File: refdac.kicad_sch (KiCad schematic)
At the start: 2 parts

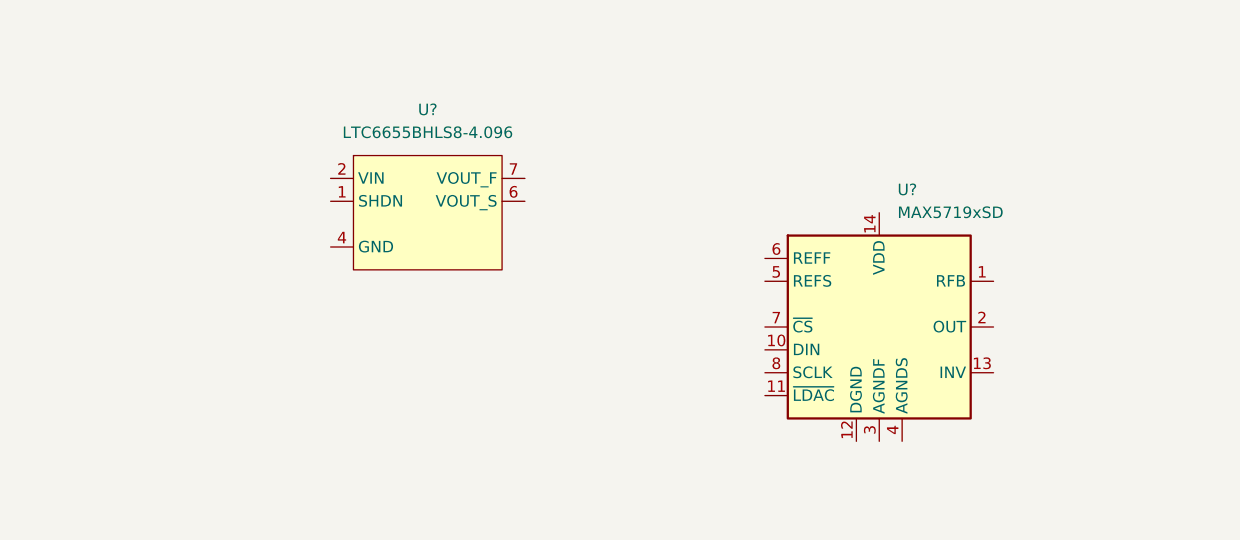
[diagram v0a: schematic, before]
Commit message: finish drive stage, add sheets
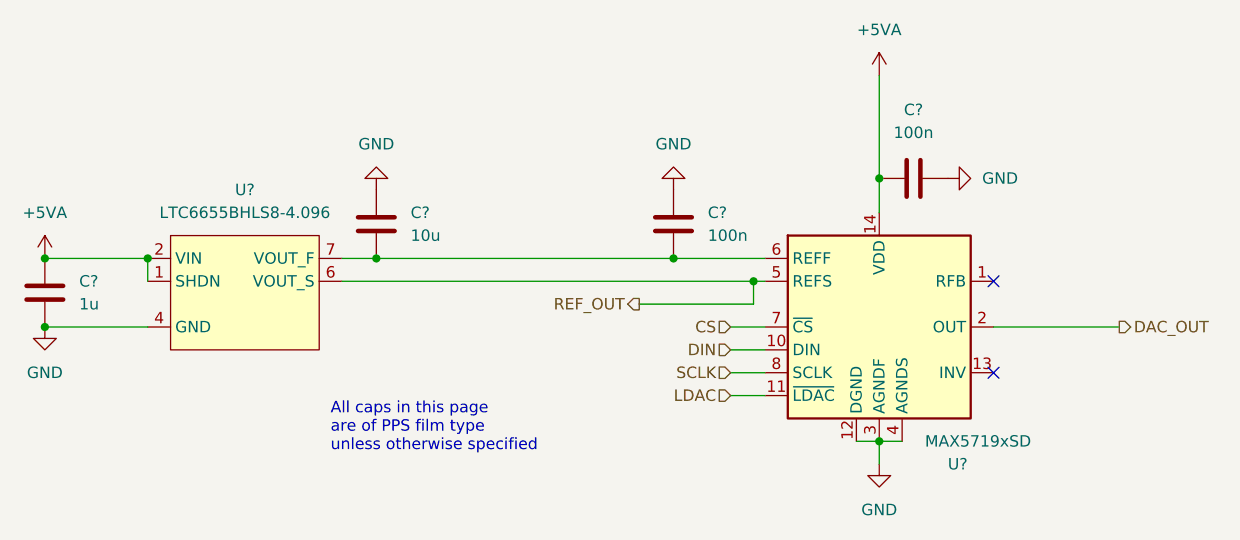
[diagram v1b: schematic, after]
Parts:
- added C? (x2): 100n, symbol Device:C
- added C?: 10u, symbol Device:C
- added C?: 1u, symbol Device:C
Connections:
- net GND: now also U?.12 (DGND), U?.3 (AGNDF), U?.4 (AGNDS), C?.1, C?.1, C?.2, C?.2
- net DIN: now reaches U?.10 (DIN)
- net LDAC: now reaches U?.11 (~{LDAC})
- net +5VA: now reaches U?.14 (VDD)
- net +5VA: now also U?.1 (SHDN), U?.2 (VIN), C?.1, C?.1
- net DAC_OUT: now reaches U?.2 (OUT)
- net REF_OUT: now reaches U?.5 (REFS)
- net REF_OUT: now also U?.6 (VOUT_S)
- net at U?.6 (REFF): now also U?.7 (VOUT_F), C?.2, C?.2
- net CS: now reaches U?.7 (~{CS})
- net SCLK: now reaches U?.8 (SCLK)
- no-connect marks 0 -> 2
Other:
- note added: "All caps in this page are of PPS film type unless otherwise specified"
- moved on the sheet: U?
